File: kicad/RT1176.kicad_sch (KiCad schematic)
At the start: 0 parts

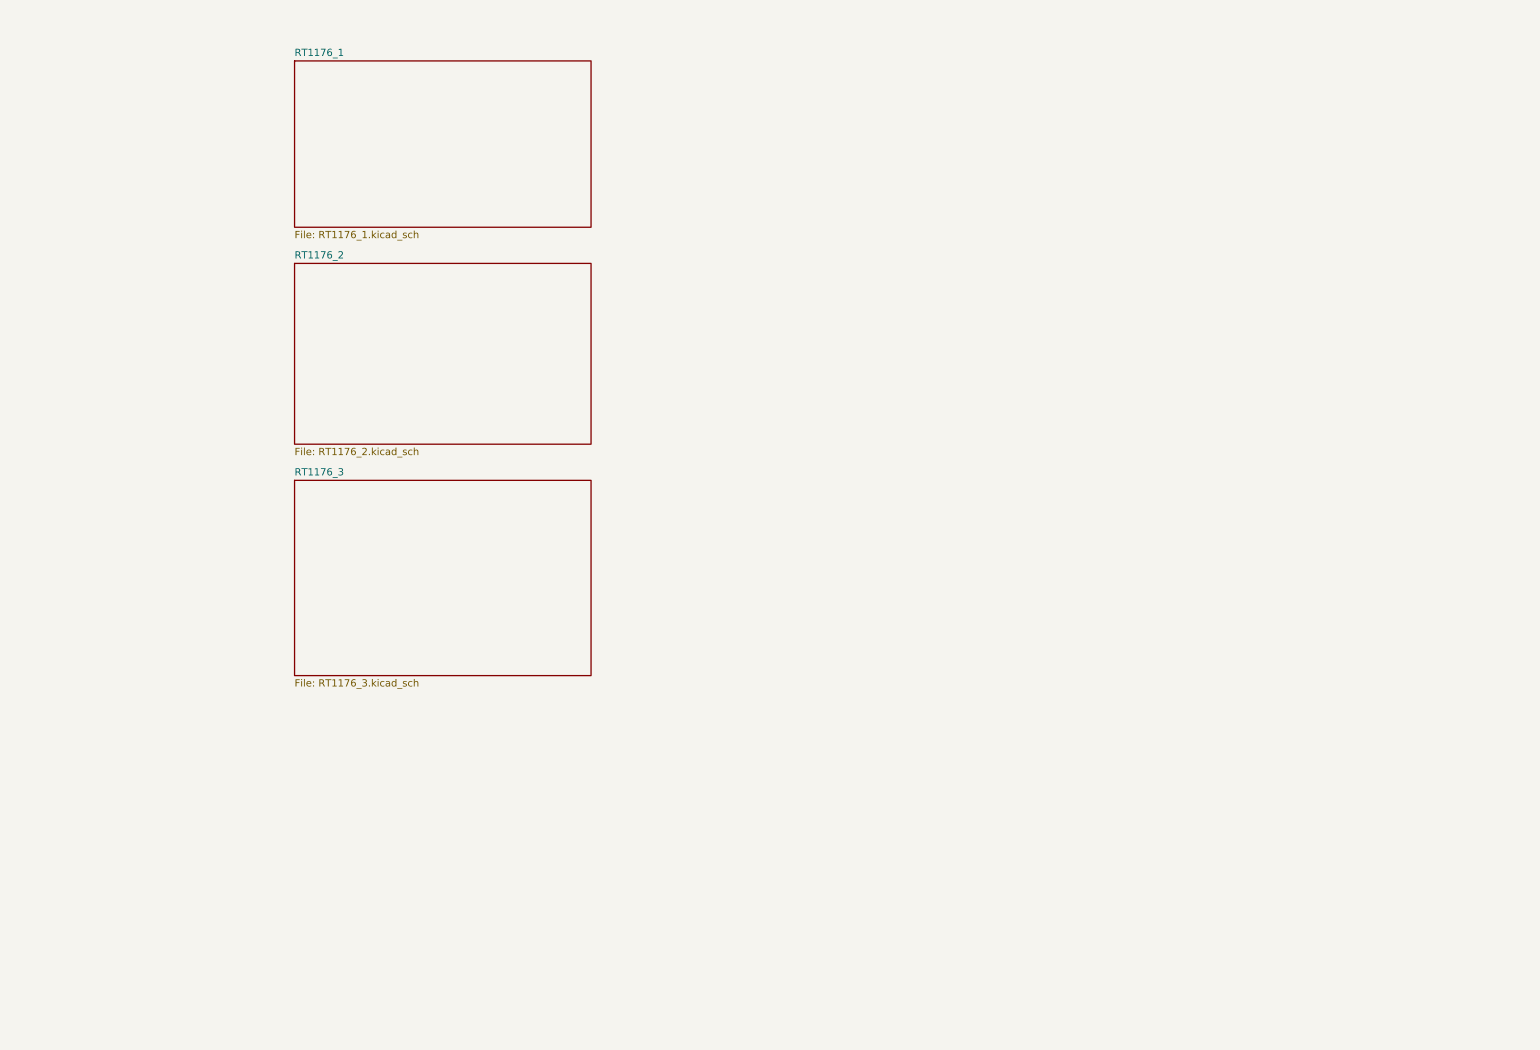
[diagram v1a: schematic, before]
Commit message: TPU 0.3.1 Production Outputs Sheet updates so it looks marginally professional Test points out the wazoo
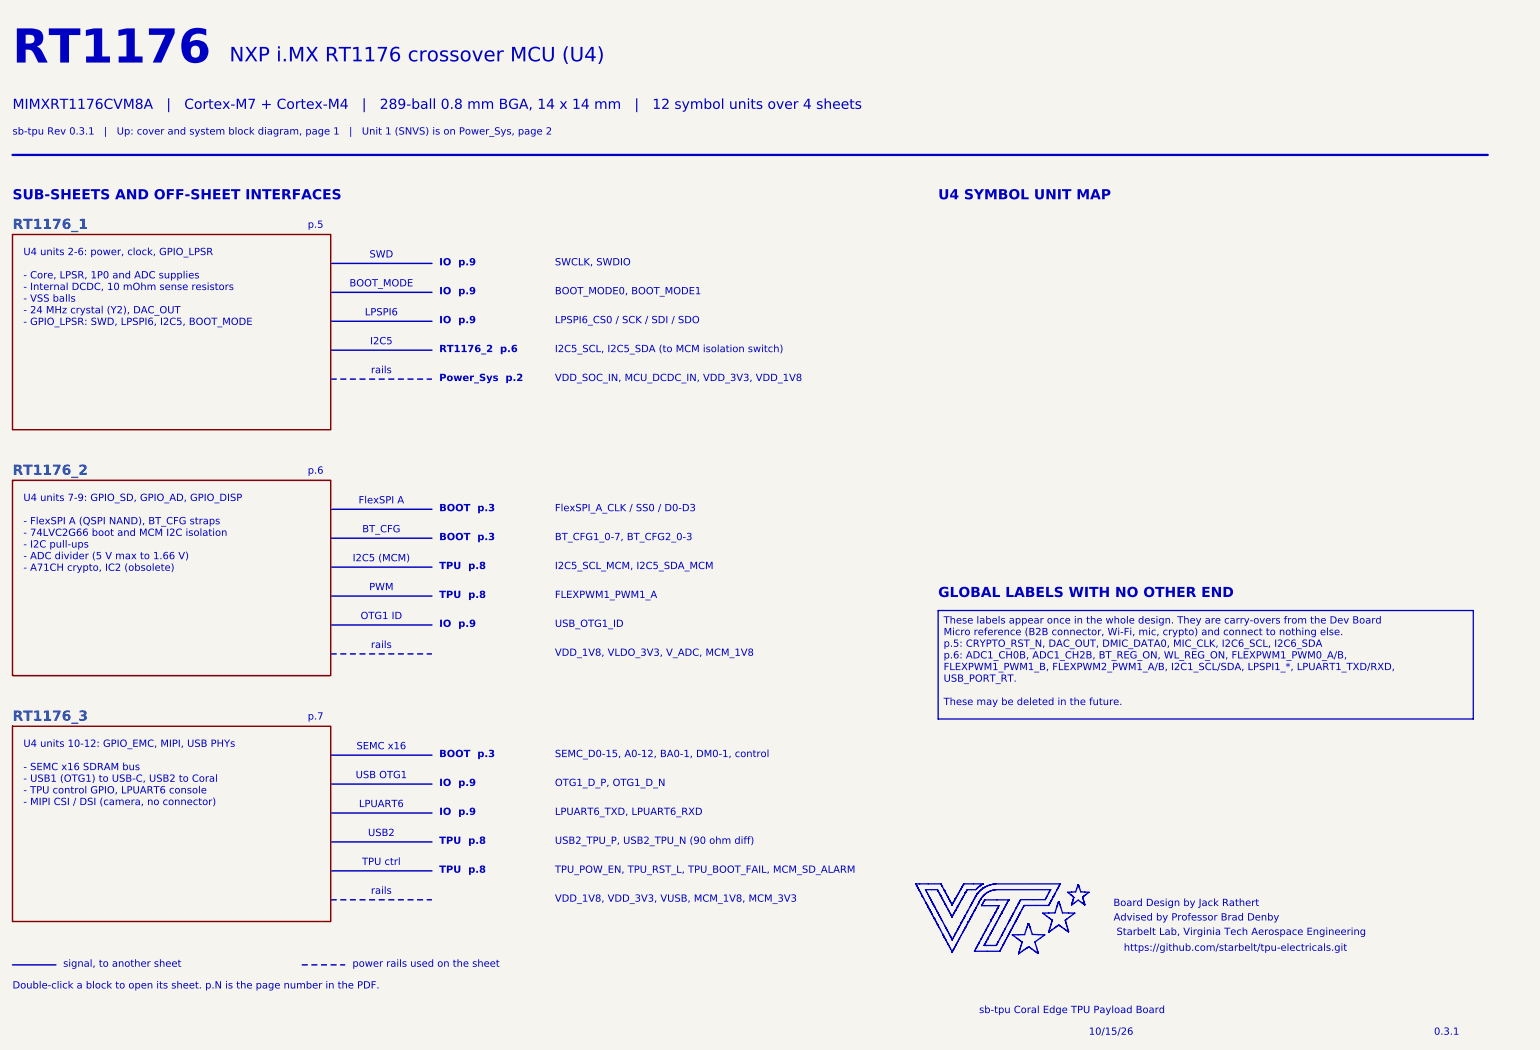
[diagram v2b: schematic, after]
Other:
- note added: "0.3.1"
- note added: "10/15/26"
- note added: "Advised by Professor Brad Denby"
- note added: "BOOT p.3"
- note added: "BOOT_MODE"
- note added: "BOOT_MODE0, BOOT_MODE1"
- note added: "BT_CFG"
- note added: "BT_CFG1_0-7, BT_CFG2_0-3"
- note added: "Board Design by Jack Rathert"
- note added: "Double-click a block to open its sheet. p.N is the page number in the PDF."
- note added: "FLEXPWM1_PWM1_A"
- note added: "FlexSPI A"
- note added: "FlexSPI_A_CLK / SS0 / D0-D3"
- note added: "GLOBAL LABELS WITH NO OTHER END"
- note added: "I2C5"
- note added: "I2C5 (MCM)"
- note added: "I2C5_SCL, I2C5_SDA (to MCM isolation switch)"
- note added: "I2C5_SCL_MCM, I2C5_SDA_MCM"
- note added: "IO p.9"
- note added: "LPSPI6"
- note added: "LPSPI6_CS0 / SCK / SDI / SDO"
- note added: "LPUART6"
- note added: "LPUART6_TXD, LPUART6_RXD"
- note added: "MIMXRT1176CVM8A | Cortex-M7 + Cortex-M4 | 289-ball 0.8 mm BGA, 14 x 14 mm | 12 symbol units over 4 sheets"
- note added: "NXP i.MX RT1176 crossover MCU (U4)"
- note added: "OTG1 ID"
- note added: "OTG1_D_P, OTG1_D_N"
- note added: "PWM"
- note added: "Power_Sys p.2"
- note added: "RT1176"
- note added: "RT1176_2 p.6"
- note added: "SEMC x16"
- note added: "SEMC_D0-15, A0-12, BA0-1, DM0-1, control"
- note added: "SUB-SHEETS AND OFF-SHEET INTERFACES"
- note added: "SWCLK, SWDIO"
- note added: "SWD"
- note added: "Starbelt Lab, Virginia Tech Aerospace Engineering"
- note added: "TPU ctrl"
- note added: "TPU p.8"
- note added: "TPU_POW_EN, TPU_RST_L, TPU_BOOT_FAIL, MCM_SD_ALARM"
- note added: "U4 SYMBOL UNIT MAP"
- note added: "U4 units 10-12: GPIO_EMC, MIPI, USB PHYs - SEMC x16 SDRAM bus - USB1 (OTG1) to USB-C, USB2 to Coral - TPU control GPIO, LPUART6 console - MIPI CSI / DSI (camera, no connector)"
- note added: "U4 units 2-6: power, clock, GPIO_LPSR - Core, LPSR, 1P0 and ADC supplies - Internal DCDC, 10 mOhm sense resistors - VSS balls - 24 MHz crystal (Y2), DAC_OUT - GPIO_LPSR: SWD, LPSPI6, I2C5, BOOT_MODE"
- note added: "U4 units 7-9: GPIO_SD, GPIO_AD, GPIO_DISP - FlexSPI A (QSPI NAND), BT_CFG straps - 74LVC2G66 boot and MCM I2C isolation - I2C pull-ups - ADC divider (5 V max to 1.66 V) - A71CH crypto, IC2 (obsolete)"
- note added: "USB OTG1"
- note added: "USB2"
- note added: "USB2_TPU_P, USB2_TPU_N (90 ohm diff)"
- note added: "USB_OTG1_ID"
- note added: "VDD_1V8, VDD_3V3, VUSB, MCM_1V8, MCM_3V3"
- note added: "VDD_1V8, VLDO_3V3, V_ADC, MCM_1V8"
- note added: "VDD_SOC_IN, MCU_DCDC_IN, VDD_3V3, VDD_1V8"
- note added: "https://github.com/starbelt/tpu-electricals.git"
- note added: "p.5"
- note added: "p.6"
- note added: "p.7"
- note added: "power rails used on the sheet"
- note added: "rails"
- note added: "sb-tpu Coral Edge TPU Payload Board"
- note added: "sb-tpu Rev 0.3.1 | Up: cover and system block diagram, page 1 | Unit 1 (SNVS) is on Power_Sys, page 2"
- note added: "signal, to another sheet"
